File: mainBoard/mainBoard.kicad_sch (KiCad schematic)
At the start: 1 part

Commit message: DRV
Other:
- added sheet DRV (drv.kicad_sch)
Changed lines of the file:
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@@
     (pin "1")
+  )
+  (sheet (at 203.2 63.5) (size 25.4 25.4) (fields_autoplaced)
+    (stroke (width 0.1524) (type solid) (color 0 0 0 0))
+    (fill (color 0 0 0 0.0000))
+    (property "Sheet name" "DRV" (id 0) (at 203.2 62.7884 0)
+      (effects (font (size 1.27 1.27)) (justify left bottom))
+    )
+    (property "Sheet file" "drv.kicad_sch" (id 1) (at 203.2 89.4846 0)
+      (effects (font (size 1.27 1.27)) (justify left top))
+    )
   )
   (sheet (at 63.5 38.1) (size 25.4 7.62) (fields_autoplaced)
@@
     (path "/64dbc0d3-4eed-460b-93d3-a846dd72318b" (page "2"))
     (path "/b14c8b1b-493a-4a02-90ea-b228e228c2ae" (page "3"))
+    (path "/007b5876-baf1-4b85-a507-5fa12bfe2ac5" (page "4"))
   )
   (symbol_instances
@@
       (reference "C?") (unit 1) (value "100n") (footprint "Capacitor_SMD:C_0402_1005Metric")
     )
+    (path "/007b5876-baf1-4b85-a507-5fa12bfe2ac5/0d52366c-5198-49dc-a226-0f46d492d233"
+      (reference "C?") (unit 1) (value "10n") (footprint "Capacitor_SMD:C_0402_1005Metric")
+    )
     (path "/b14c8b1b-493a-4a02-90ea-b228e228c2ae/1d544ee4-261a-4a09-b586-b3ed4dcf6574"
       (reference "C?") (unit 1) (value "2u2") (footprint "Capacitor_SMD:C_0402_1005Metric")
@@
     (path "/64dbc0d3-4eed-460b-93d3-a846dd72318b/2ae71f77-4ba2-42fa-bcee-7f3f15bdd4b7"
       (reference "C?") (unit 1) (value "1u") (footprint "Inductor_SMD:L_0805_2012Metric")
+    )
+    (path "/007b5876-baf1-4b85-a507-5fa12bfe2ac5/3526c070-dfbf-4d9d-8530-a1ed7705375f"
+      (reference "C?") (unit 1) (value "22u") (footprint "Capacitor_SMD:C_2220_5650Metric")
     )
     (path "/b14c8b1b-493a-4a02-90ea-b228e228c2ae/5f21e47f-1776-439c-a4bd-dddc237b4ce9"
@@
       (reference "C?") (unit 1) (value "1u") (footprint "Inductor_SMD:L_0805_2012Metric")
     )
+    (path "/007b5876-baf1-4b85-a507-5fa12bfe2ac5/31ff19c9-8a05-4d75-9c75-1f35cf368e66"
+      (reference "J?") (unit 1) (value "Conn_01x01") (footprint "")
+    )
+    (path "/007b5876-baf1-4b85-a507-5fa12bfe2ac5/39245b7c-706c-4904-890f-add57fdfda2c"
+      (reference "J?") (unit 1) (value "Conn_01x01") (footprint "")
+    )
     (path "/4709a3ec-d1a9-46f6-9b20-447e28f2ef2a"
       (reference "J?") (unit 1) (value "Conn_01x07") (footprint "")
@@
       (reference "L?") (unit 1) (value "33u") (footprint "Inductor_SMD:L_1008_2520Metric")
     )
+    (path "/007b5876-baf1-4b85-a507-5fa12bfe2ac5/2d9a62f4-f6de-43ae-a6ea-13aef4f22444"
+      (reference "R?") (unit 1) (value "1k") (footprint "Capacitor_SMD:C_0402_1005Metric")
+    )
     (path "/64dbc0d3-4eed-460b-93d3-a846dd72318b/258dde30-2273-432d-9899-bc1f39124052"
       (reference "U?") (unit 1) (value "MAX15062A") (footprint "Package_DFN_QFN:DFN-8_2x2mm_P0.5mm")
@@
       (reference "U?") (unit 1) (value "STM32H503CBT6") (footprint "Package_QFP:LQFP-48-1EP_7x7mm_P0.5mm_EP3.6x3.6mm")
     )
+    (path "/007b5876-baf1-4b85-a507-5fa12bfe2ac5/e78b8369-9a65-474a-a997-cb1d4c7b41a6"
+      (reference "U?") (unit 1) (value "DRV8251ADDAR") (footprint "Package_SO:SOIC-8-1EP_3.9x4.9mm_P1.27mm_EP2.62x3.51mm_ThermalVias")
+    )
   )

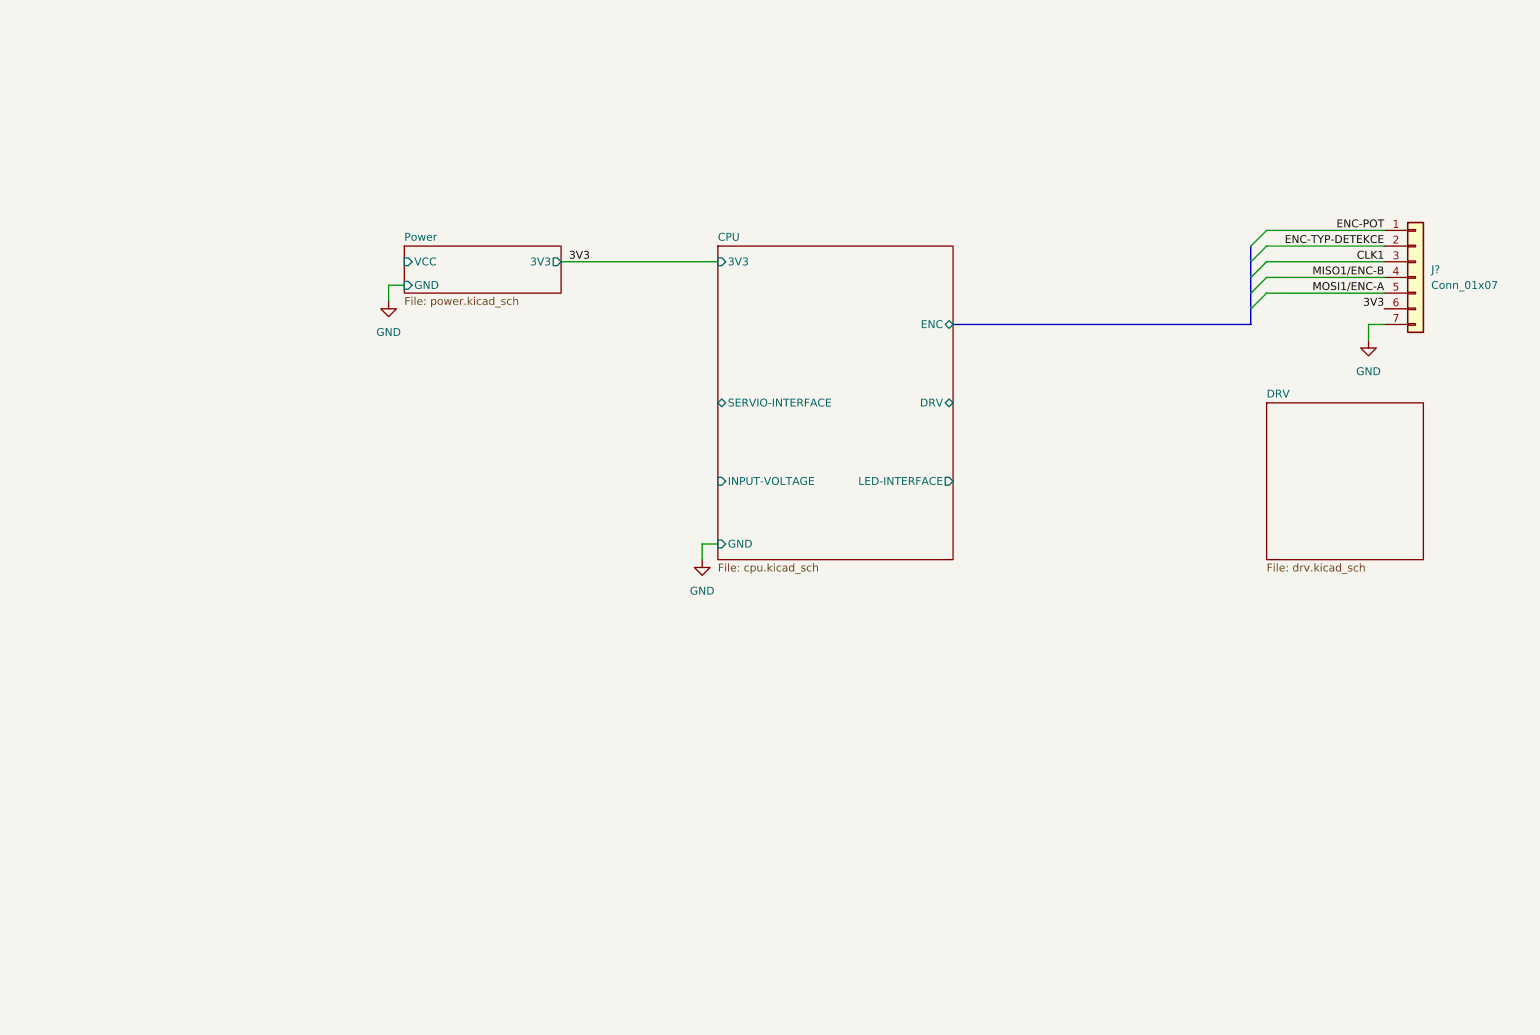
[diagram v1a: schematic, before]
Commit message: LEDky, měření napájení, připojení DRV atd.
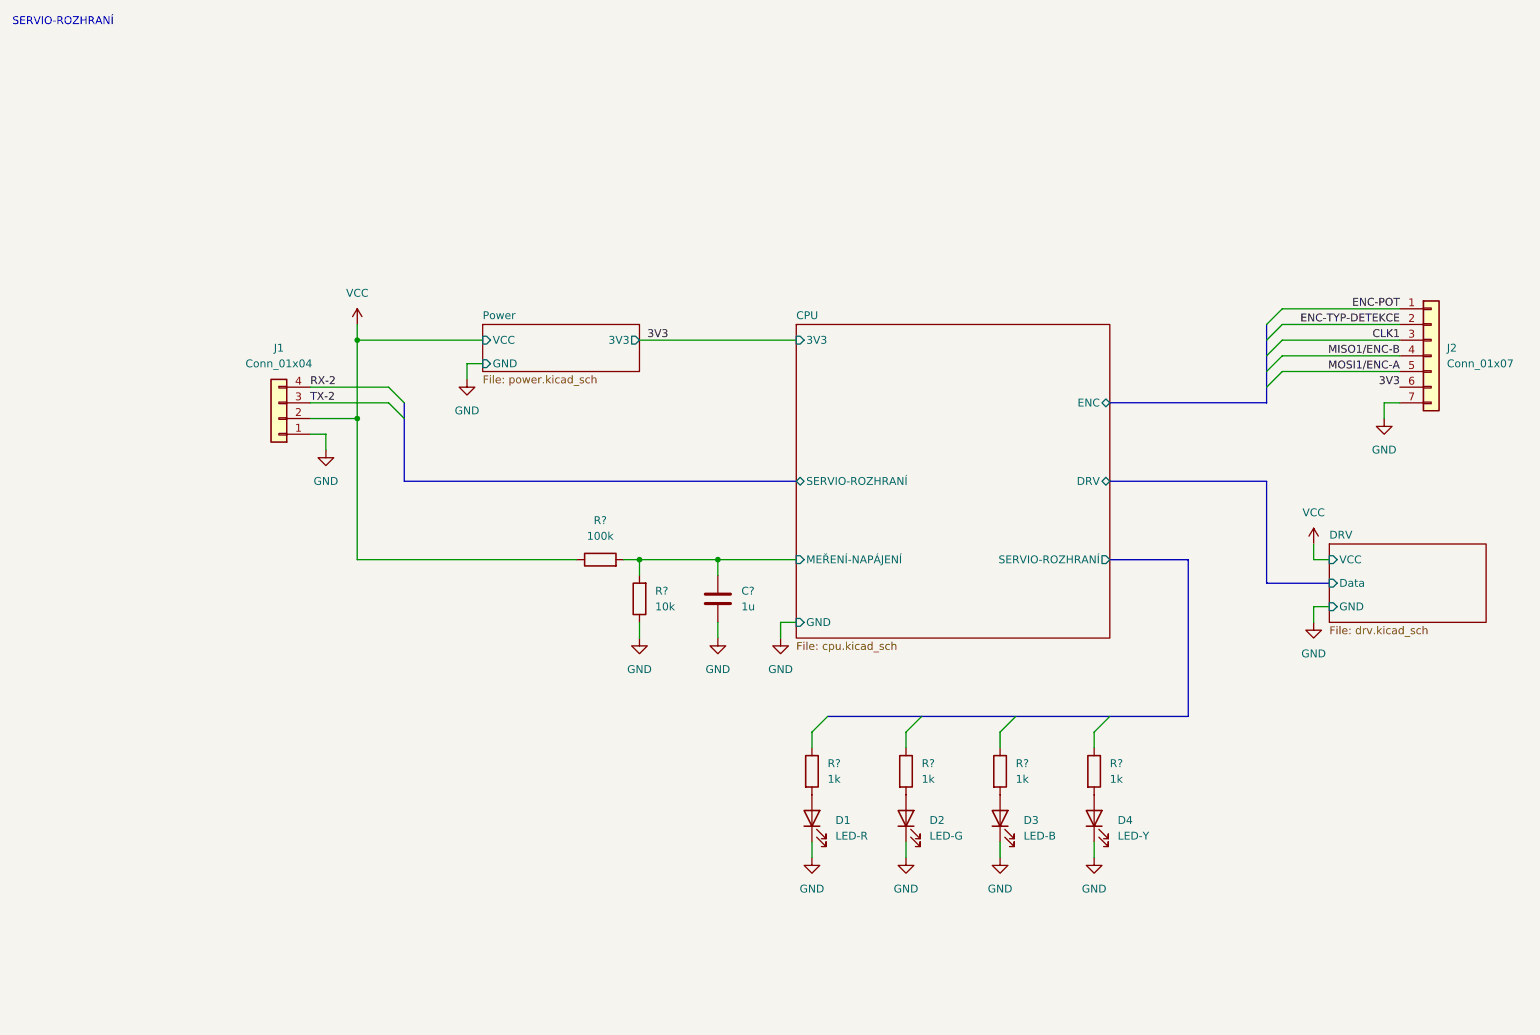
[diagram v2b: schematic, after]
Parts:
- added C?: 1u, Capacitor_SMD:C_0402_1005Metric, symbol Device:C
- added D1: LED-R, LED_SMD:LED_0603_1608Metric, symbol Device:LED
- added D2: LED-G, LED_SMD:LED_0603_1608Metric, symbol Device:LED
- added D3: LED-B, LED_SMD:LED_0603_1608Metric, symbol Device:LED
- added D4: LED-Y, LED_SMD:LED_0603_1608Metric, symbol Device:LED
- added J1: Conn_01x04, symbol Connector_Generic:Conn_01x04
- added R?: 10k, Capacitor_SMD:C_0402_1005Metric, symbol Device:R
- added R? (x4): 1k, Capacitor_SMD:C_0402_1005Metric, symbol Device:R
- added R?: 100k, Capacitor_SMD:C_0402_1005Metric, symbol Device:R
- gave numbers to parts that had none: 1
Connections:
- net GND: now also C?.2, D1.1 (K), D2.1 (K), D3.1 (K), D4.1 (K), J1.1 (Pin_1), R?.1
- new net: D3.2 (A), R?.2
- new net: D4.2 (A), R?.2
- new net: D2.2 (A), R?.2
- new net: D1.2 (A), R?.2
- new net CPU/MEŘENÍ-NAPÁJENÍ: C?.1, R?.2, R?.2
- new net RX-2: J1.4 (Pin_4)
- new net TX-2: J1.3 (Pin_3)
- new net VCC: J1.2 (Pin_2), R?.1
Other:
- sheet CPU ports: added MEŘENÍ-NAPÁJENÍ, SERVIO-ROZHRANÍ; removed INPUT-VOLTAGE, LED-INTERFACE, SERVIO-INTERFACE
- sheet DRV ports: added Data, GND, VCC; removed none
- note added: "SERVIO-ROZHRANÍ"
- moved on the sheet: J2

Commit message: Pouzdra
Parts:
- added J2: Conn_01x04, Connector_JST:JST_XH_B4B-XH-AM_1x04_P2.50mm_Vertical, symbol Connector_Generic:Conn_01x04
- J1: footprint (none) -> Connector_JST:JST_XH_B4B-XH-AM_1x04_P2.50mm_Vertical
- J6: renamed from J2; footprint (none) -> Connector_JST:JST_XH_B8B-XH-AM_1x08_P2.50mm_Vertical
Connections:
- net GND: now also J2.1 (Pin_1)
- net RX-2: now also J2.4 (Pin_4)
- net TX-2: now also J2.3 (Pin_3)
- net VCC: now also J2.2 (Pin_2)
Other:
- moved on the sheet: J1

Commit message: test-pointy a zdvojení konektorů
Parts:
- added J7: Conn_01x07, Connector_PinHeader_1.00mm:PinHeader_1x07_P1.00mm_Horizontal, symbol Connector_Generic:Conn_01x07
- J6: footprint Connector_JST:JST_XH_B8B-XH-AM_1x08_P2.50mm_Vertical -> Connector_JST:JST_XH_B7B-XH-AM_1x07_P2.50mm_Vertical
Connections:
- net 3V3: now also J7.6 (Pin_6)
- net CLK1: now also J7.3 (Pin_3)
- net ENC-POT: now also J7.1 (Pin_1)
- net ENC-TYP-DETEKCE: now also J7.2 (Pin_2)
- net GND: now also J7.7 (Pin_7)
- net MISO1/ENC-B: now also J7.4 (Pin_4)
- net MOSI1/ENC-A: now also J7.5 (Pin_5)
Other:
- moved on the sheet: C?, D1, D2, D3, D4, J1, J2, J6, R?
